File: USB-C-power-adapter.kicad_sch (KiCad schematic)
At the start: 61 parts, among them J1 JST_SH_1x4_SM04B-SRSS-TB-LF-SN, J2 Molex_Nano-Fit_1x2_105313-220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, J3 USB-C_GCT_USB4105-GF-A, Q1 SQS401EN-T1_BE3, U1 TPD4E02B04DQA, U2 TPD4E02B04DQA, U3 STUSB4500_QFN, U4 SIC477ED-T1-GE3

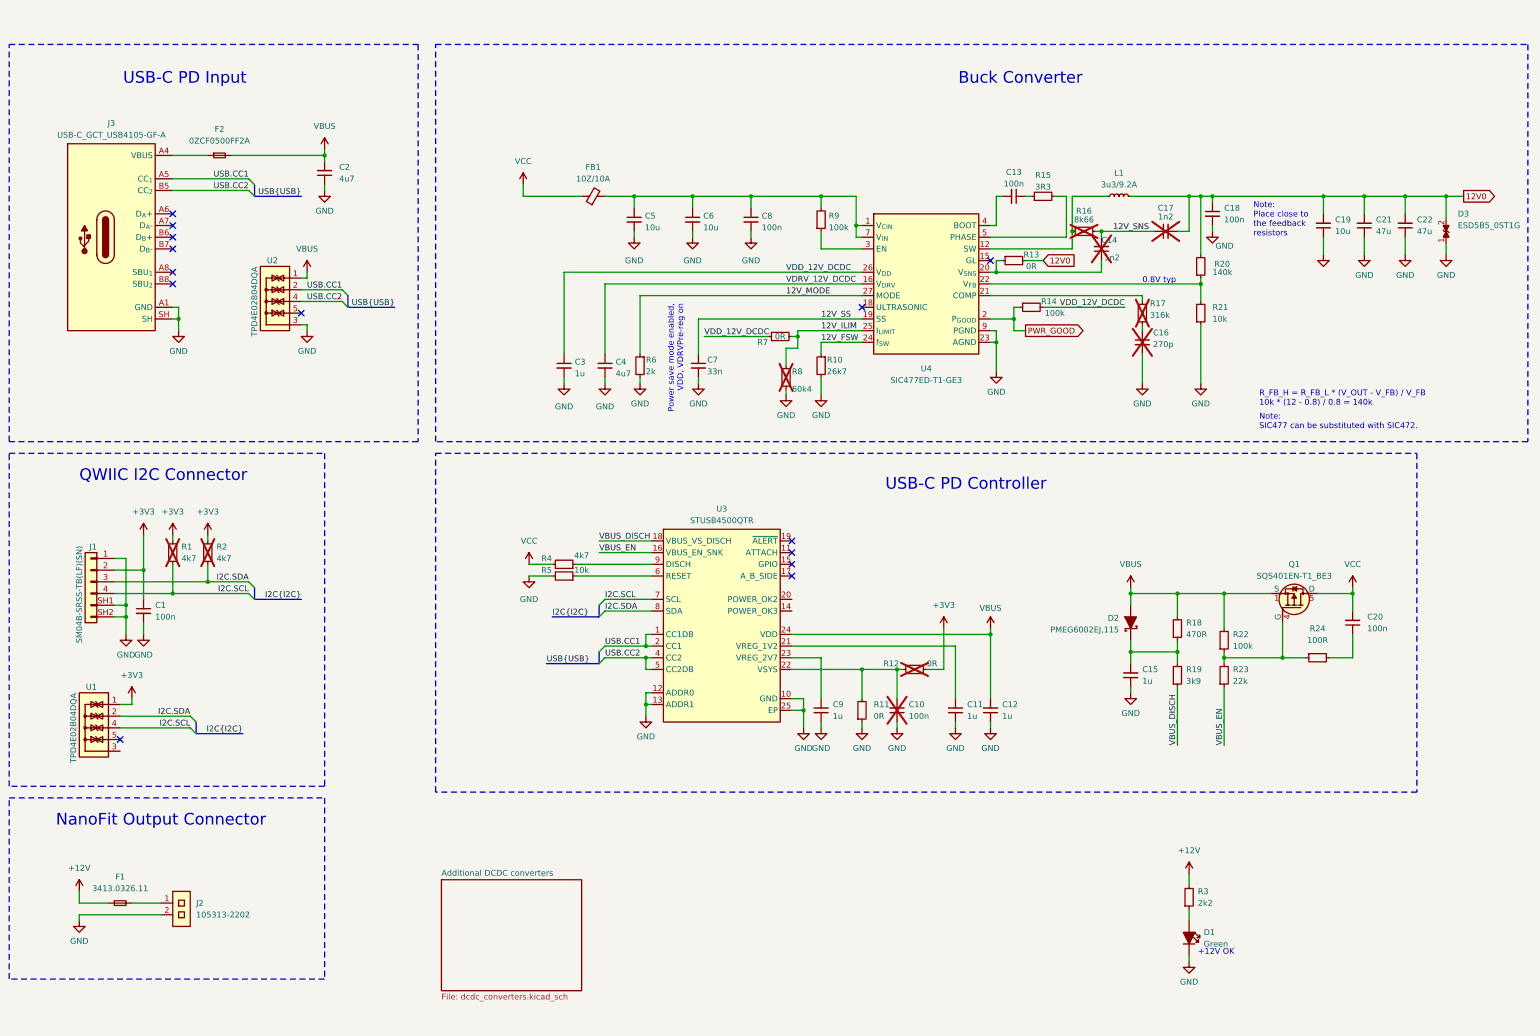
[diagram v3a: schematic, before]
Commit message: [#57006] Move connectors to separate sheet
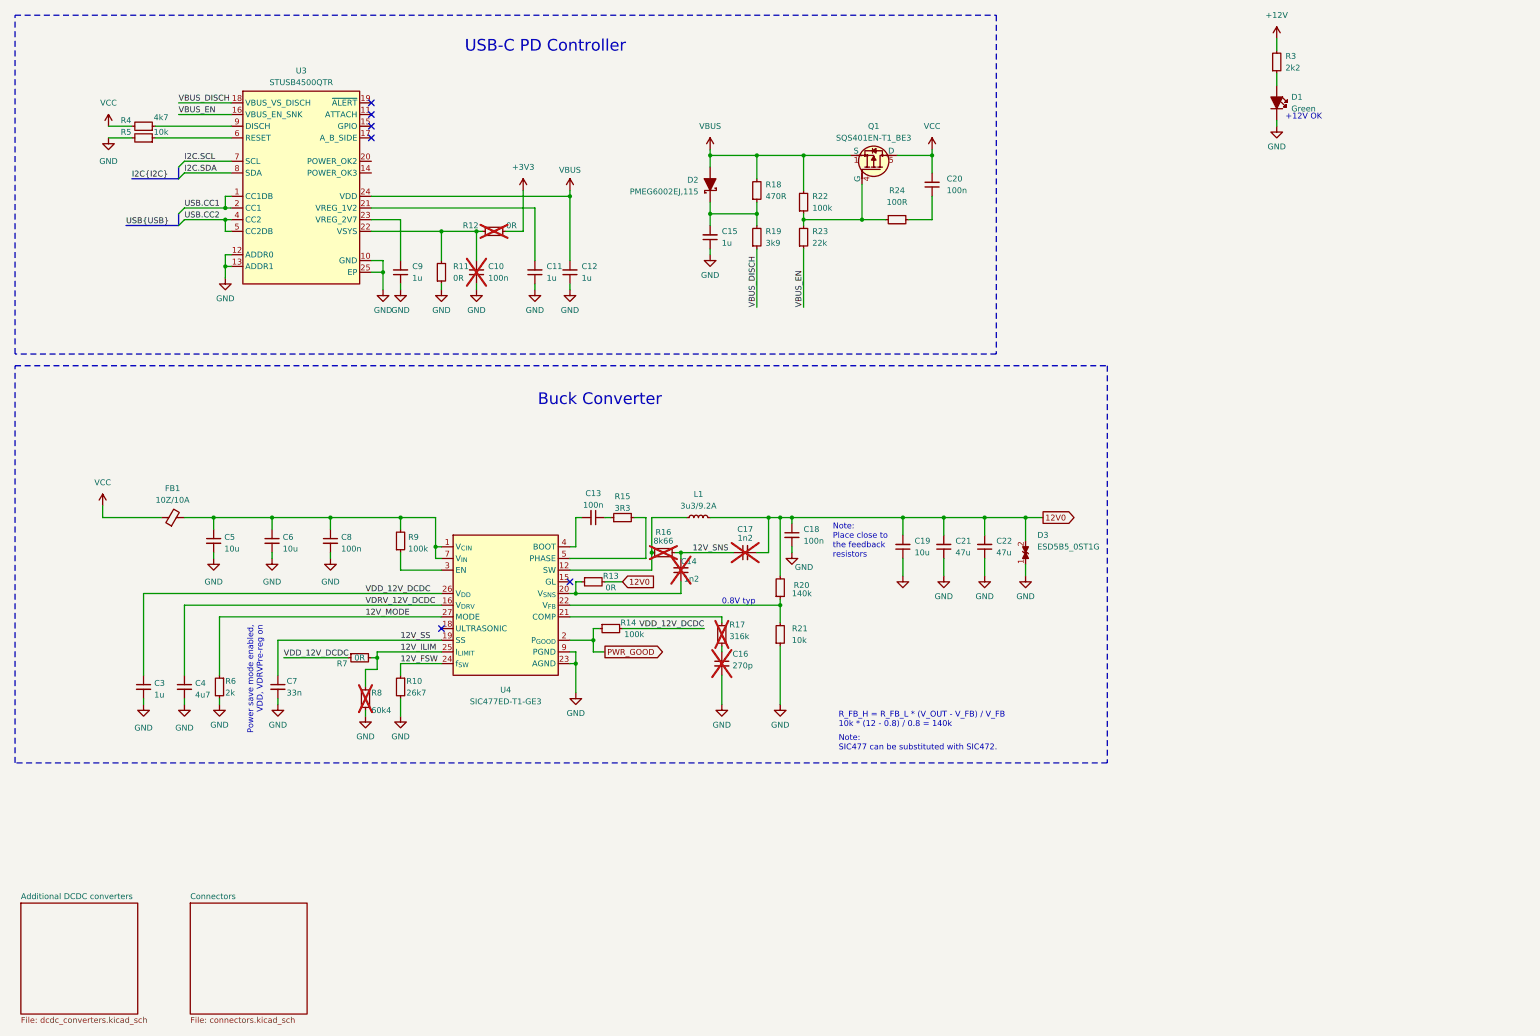
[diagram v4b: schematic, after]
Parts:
- removed C1: C_100n_16V_X7R_0402, antmicro-footprints:C_0402_1005Metric, symbol antmicroCapacitors0402:C_100n_16V_X7R_0402
- removed C2: C_4u7_25V_0402, antmicro-footprints:C_0402_1005Metric, symbol antmicroCapacitors0402:C_4u7_25V_0402
- removed F1: F_7A_1206, antmicro-footprints:F_1206_3216Metric, symbol antmicroFuses:F_7A_1206
- removed F2: F_5A_2920, antmicro-footprints:2920-fuse, symbol antmicroFuses:F_5A_2920
- removed J1: JST_SH_1x4_SM04B-SRSS-TB-LF-SN, antmicro-footprints:Conn_JST_SH_1x4_SM04B-SRSS-TB-LF-SN, symbol antmicroWire2BoardConnectors:JST_SH_1x4_SM04B-SRSS-TB-LF-SN
- removed J2: Molex_Nano-Fit_1x2_105313-2202_Horizontal, antmicro-footprints:Conn_Molex_Nano-Fit_1x2_105313-2202_Horizontal, symbol antmicroWire2BoardConnectors:Molex_Nano-Fit_1x2_105313-2202_Horizontal
- removed J3: USB-C_GCT_USB4105-GF-A, antmicro-footprints:USB-C_Receptacle_GCT_USB4105-GF-A, symbol antmicroUSBConnectors:USB-C_GCT_USB4105-GF-A
- removed R1, R2: R_4k7_0402, antmicro-footprints:R_0402_1005Metric, symbol antmicroResistors0402:R_4k7_0402
- removed U1, U2: TPD4E02B04DQA, antmicro-footprints:USON-10_2.5x1mm_P0.5mm, symbol antmicroTVSDiodes:TPD4E02B04DQA
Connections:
- no-connect marks 14 -> 6
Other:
- added sheet Connectors (connectors.kicad_sch)
- note removed: "NanoFit Output Connector"
- note removed: "QWIIC I2C Connector"
- note removed: "USB-C PD Input"
- moved on the sheet: C10, C11, C12, C13, C14, C15, C16, C17, C18, C19, C20, C21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

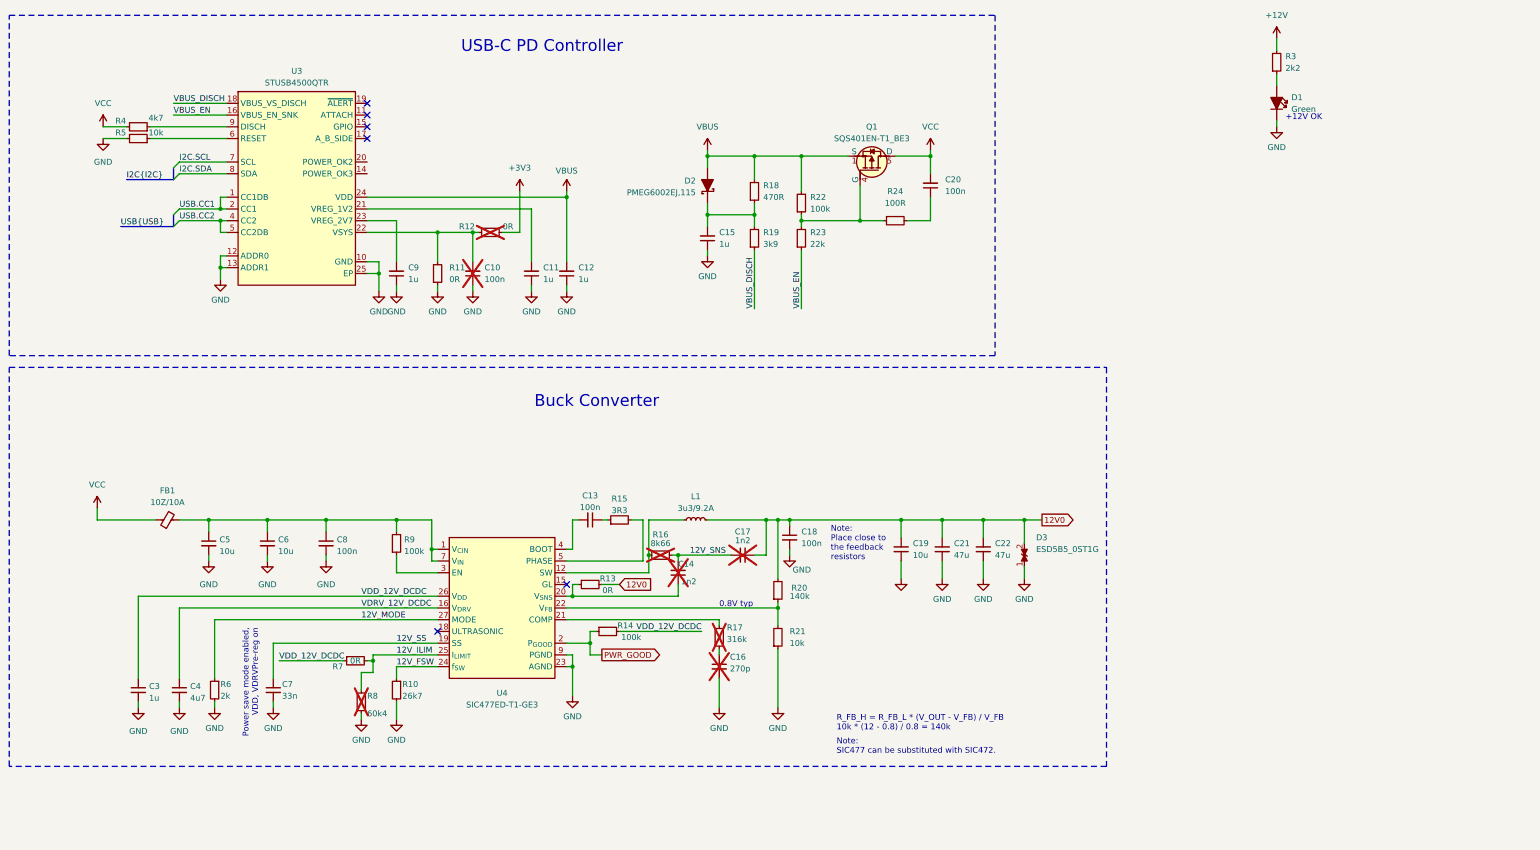
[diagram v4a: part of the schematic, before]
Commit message: [#57006] Change C17, R25, R26
Improve connections
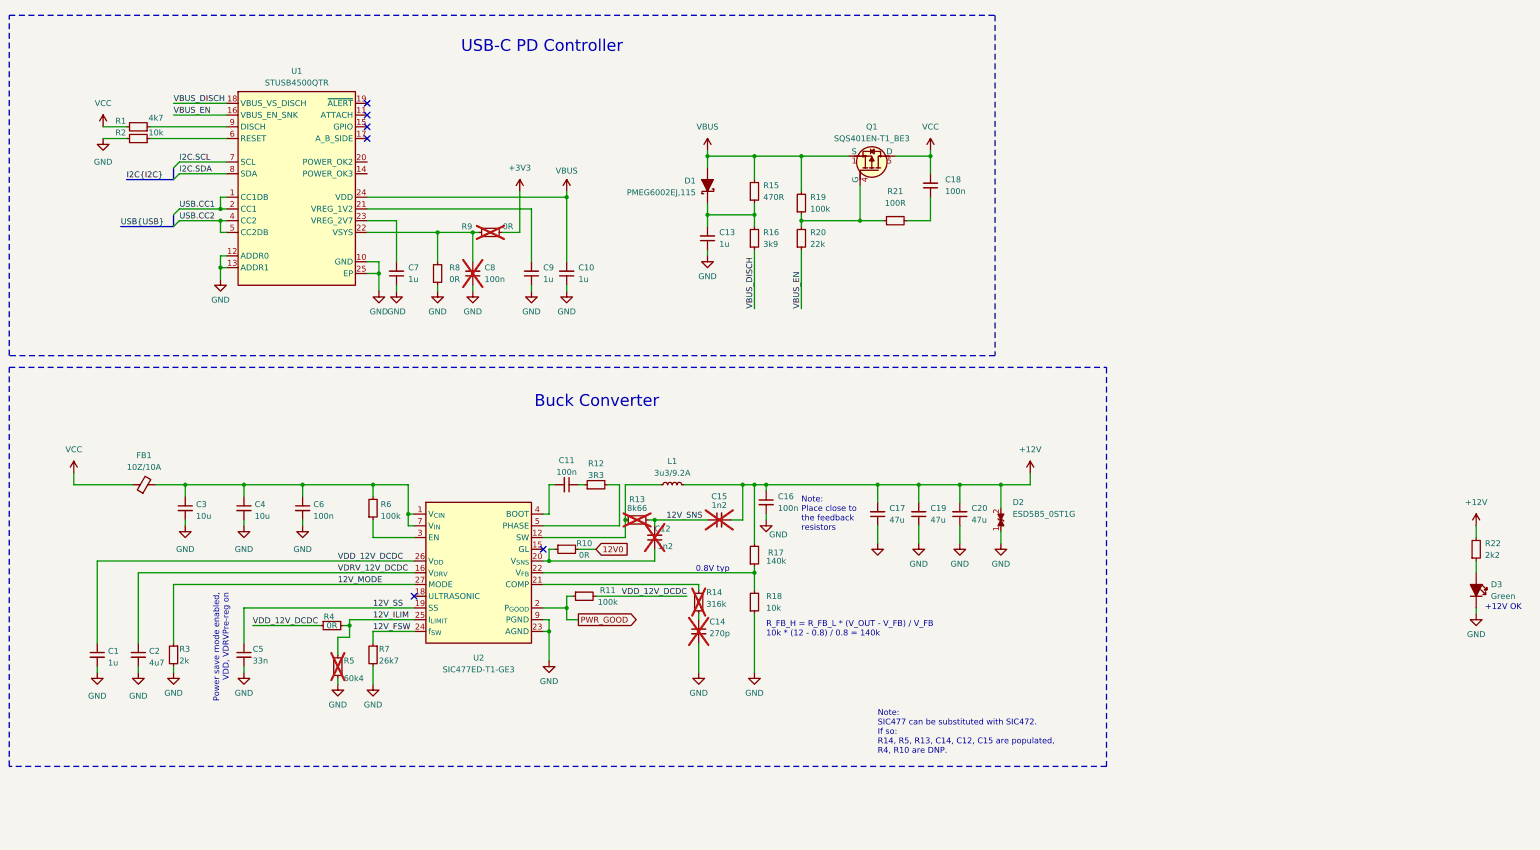
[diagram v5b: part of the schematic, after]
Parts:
- removed C19: C_10u_25V_0603, antmicro-footprints:C_0603_1608Metric, symbol antmicroCapacitors0603:C_10u_25V_0603
- added C17: C_47u_16V_1206, antmicro-footprints:C_1206_3216Metric, symbol antmicroCapacitorsmisc:C_47u_16V_1206
- renumbered C3 to C1, C12 to C10, C13 to C11, C14 to C12, C15 to C13, C16 to C14, C17 to C15, C18 to C16, C20 to C18, C21 to C19, C4 to C2, C22 to C20, C5 to C3, C6 to C4, C7 to C5, C8 to C6, C9 to C7, C10 to C8, C11 to C9, D2 to D1, D3 to D2, D1 to D3, R4 to R1, R13 to R10, R14 to R11, R15 to R12, R16 to R13, R17 to R14, R18 to R15, R19 to R16, R20 to R17, R21 to R18, R22 to R19, R5 to R2, R23 to R20, R24 to R21, R3 to R22, R6 to R3, R7 to R4, R8 to R5, R9 to R6, R10 to R7, R11 to R8, R12 to R9, U3 to U1, U4 to U2
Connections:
- net +12V: now also C15.2, C16.1, C19.2, C20.2, D2.2, L1.2, R17.2, C17.2
- net 12V0: no longer C15.2, C16.1, C19.2, C20.2, D2.2, L1.2, R17.2
- net GND: now also C17.1
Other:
- note added: "Note: SIC477 can be substituted with SIC472. If so: R14, R5, R13, C14, C12, C15 are populated, R4, R10 are DNP."
- note removed: "Note: SIC477 can be substituted with SIC472."
- moved on the sheet: C1, C11, C12, C14, C15, C16, C19, C2, C20, C3, C4, C5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

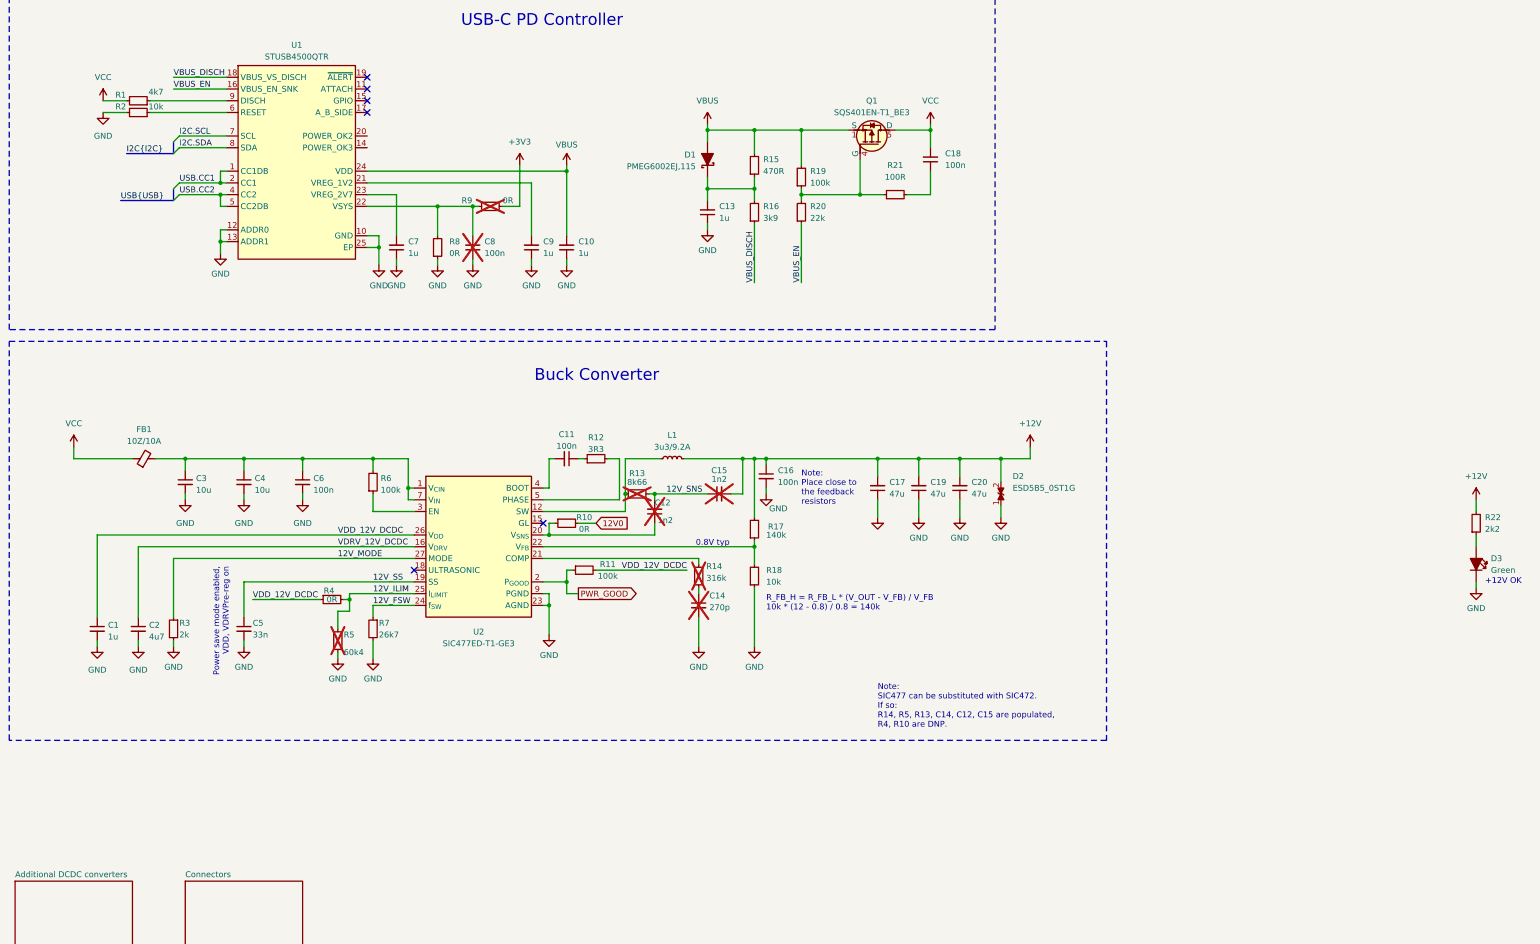
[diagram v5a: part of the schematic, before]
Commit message: [#57006] Add assembly variant selector
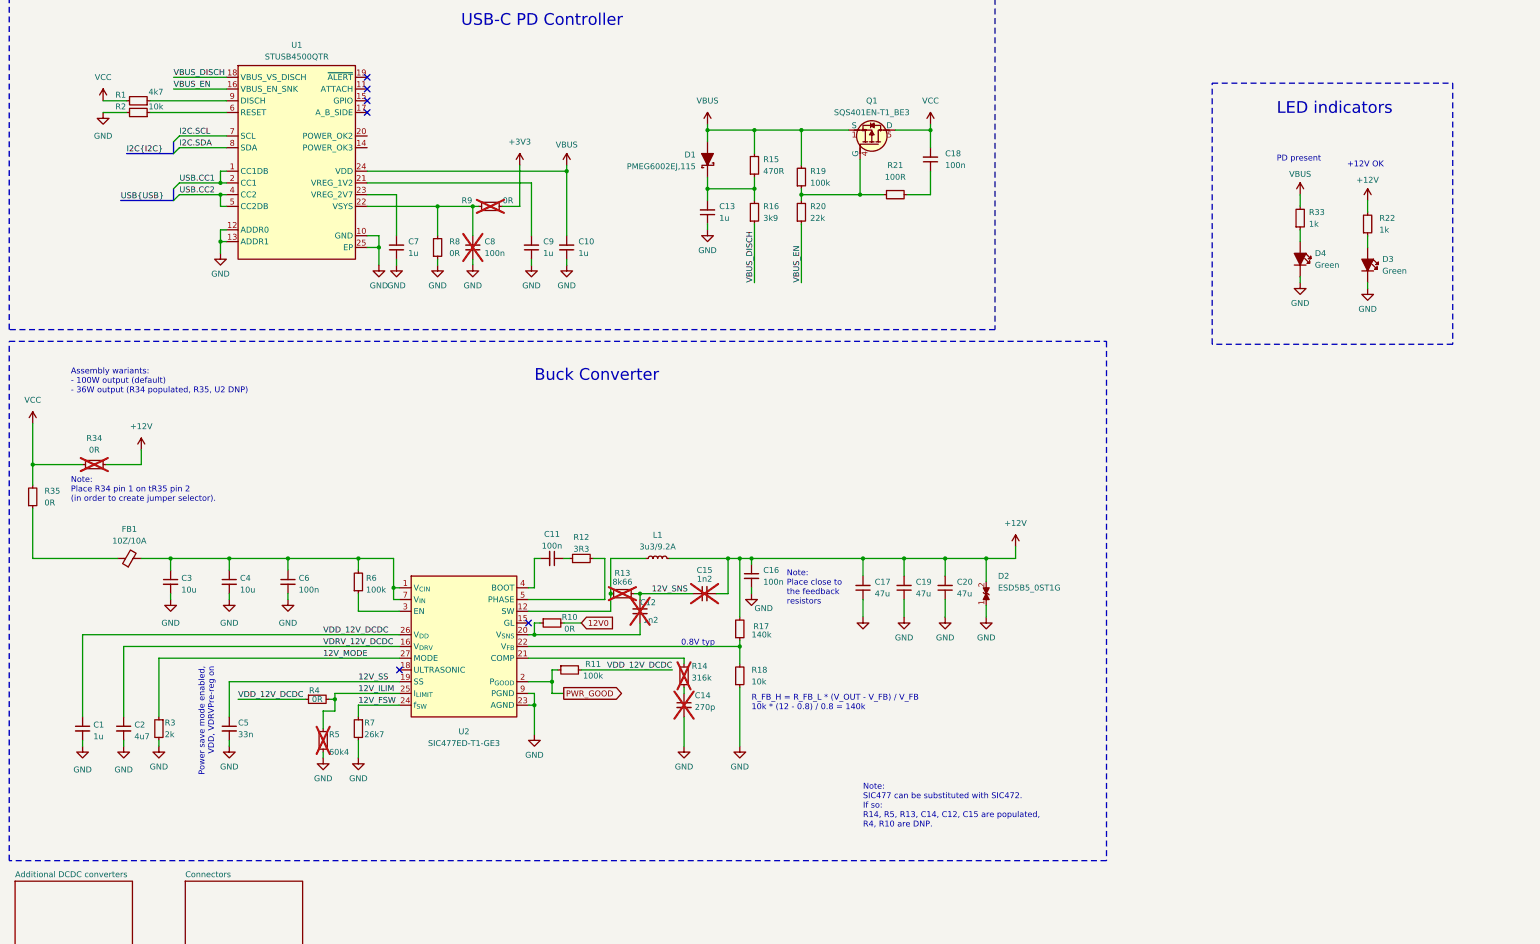
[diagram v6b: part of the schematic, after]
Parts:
- removed R22: R_2k2_0402, antmicro-footprints:R_0402_1005Metric, symbol antmicroResistors0402:R_2k2_0402
- added D4: LED_G_0603_LG_L29K-G2J1-24-Z, antmicro-footprints:LED_0603_1608Metric_G, symbol antmicroLEDIndicationDiscrete:LED_G_0603_LG_L29K-G2J1-24-Z
- added R22, R33: R_2k2_0402, antmicro-footprints:R_0402_1005Metric, symbol antmicroResistors0402:R_1k_0402
- added R34, R35: R_0R_0805, antmicro-footprints:R_0805_2012Metric, symbol antmicroResistorsmisc:R_0R_0805
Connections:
- net +12V: now also R22.2, R34.2
- net GND: now also D4.2
- net VBUS: now also R33.2
- net VCC: now also R34.1, R35.2; no longer FB1.1
- net at D3.1: now also R22.1
- new net: FB1.1, R35.1
- new net: D4.1, R33.1
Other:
- note added: "Assembly wariants: - 100W output (default) - 36W output (R34 populated, R35, U2 DNP)"
- note added: "LED indicators"
- note added: "Note: Place R34 pin 1 on tR35 pin 2 (in order to create jumper selector)."
- note added: "PD present"
- moved on the sheet: C1, C11, C12, C14, C15, C16, C17, C19, C2, C20, C3, C4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
